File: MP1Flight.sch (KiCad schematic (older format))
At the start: 43 parts, among them J3 Micro_SD_Card_Det, J6 Conn_01x04_Male, J7 Screw_Terminal_01x02, SW1 SW_Push, U1 MPU-9250, U2 VisionSOM-STM32MP1

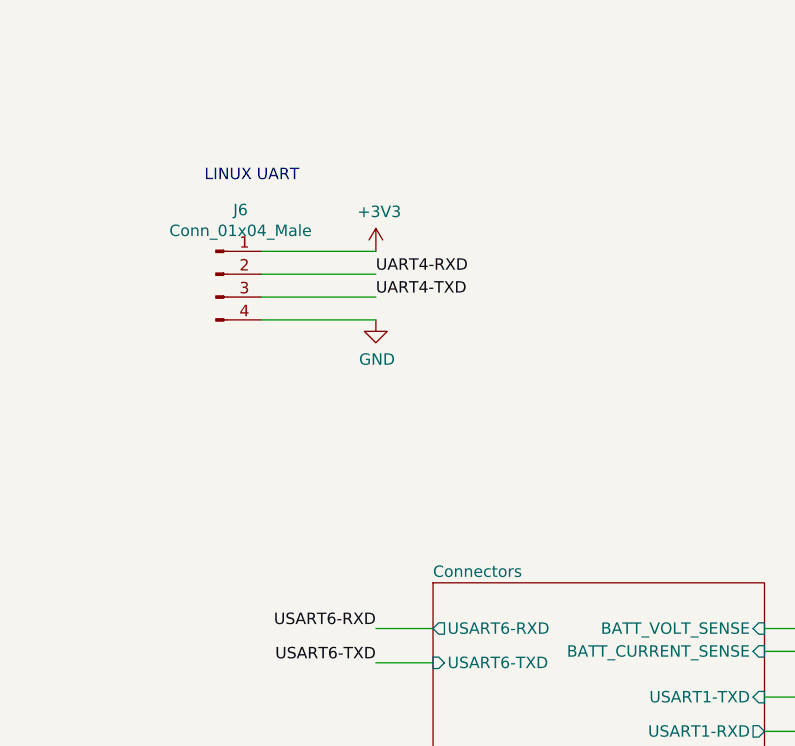
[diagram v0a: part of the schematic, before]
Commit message: Added in Debug sheet
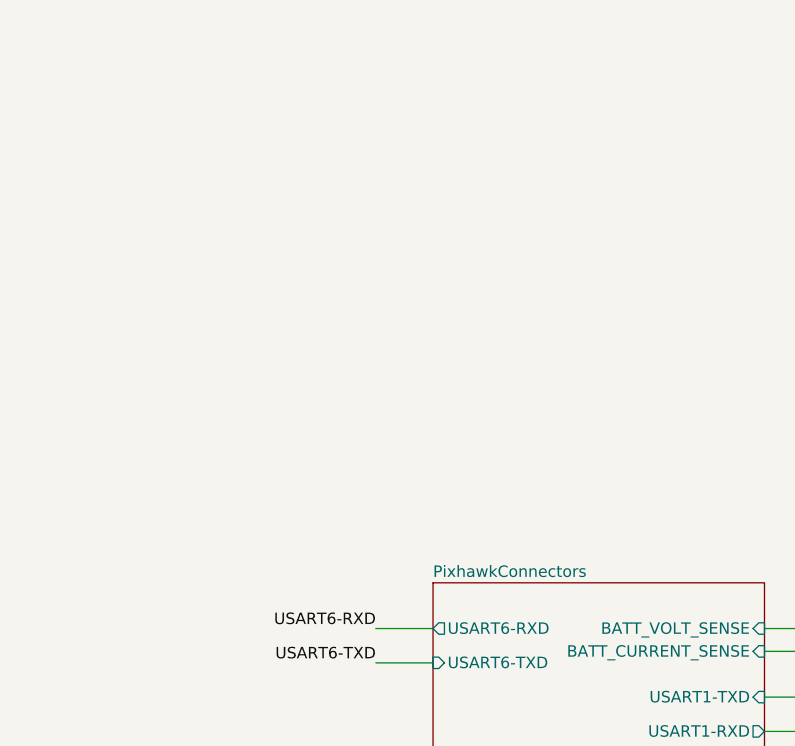
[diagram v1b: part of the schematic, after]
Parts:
- removed J6: Conn_01x04_Male, symbol Connector:Conn_01x04_Male
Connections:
- wire segments 152 -> 148
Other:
- note removed: "LINUX UART"
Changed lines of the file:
@@
 Text Notes 15500 9750 0    50   ~ 0
 LCD NOT BEING USED
-Text Label 2100 7150 0    50   ~ 0
-UART4-TXD
-Text Label 2100 7050 0    50   ~ 0
-UART4-RXD
-$Comp
-L power:+3V3 #PWR0149
-U 1 1 5EF84678
-P 2100 6950
-F 0 "#PWR0149" H 2100 6800 50  0001 C CNN
-F 1 "+3V3" H 2115 7123 50  0000 C CNN
-F 2 "" H 2100 6950 50  0001 C CNN
-F 3 "" H 2100 6950 50  0001 C CNN
-	1    2100 6950
-	1    0    0    -1
-$EndComp
-$Comp
-L power:GND #PWR0148
-U 1 1 5EF827E4
-P 2100 7250
-F 0 "#PWR0148" H 2100 7000 50  0001 C CNN
-F 1 "GND" H 2105 7077 50  0000 C CNN
-F 2 "" H 2100 7250 50  0001 C CNN
-F 3 "" H 2100 7250 50  0001 C CNN
-	1    2100 7250
-	1    0    0    -1
-$EndComp
-Wire Wire Line
-	1600 7250 2100 7250
-Wire Wire Line
-	1600 7150 2100 7150
-Wire Wire Line
-	1600 7050 2100 7050
-Wire Wire Line
-	1600 6950 2100 6950
-Text Notes 1350 6650 0    50   ~ 0
-LINUX UART
-$Comp
-L Connector:Conn_01x04_Male J6
-U 1 1 5EF08DF3
-P 1400 7050
-F 0 "J6" H 1508 7331 50  0000 C CNN
-F 1 "Conn_01x04_Male" H 1508 7240 50  0000 C CNN
-F 2 "" H 1400 7050 50  0001 C CNN
-F 3 "~" H 1400 7050 50  0001 C CNN
-	1    1400 7050
-	1    0    0    -1
-$EndComp
 $Sheet
 S 1550 2550 1350 1850
@@
 S 2350 8400 1450 1550
 U 5ED8E7B0
-F0 "Connectors" 50
+F0 "PixhawkConnectors" 50
 F1 "Connectors.sch" 50
 F2 "USART1-TXD" I R 3800 8900 50

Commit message: Added in SD Card Sheet plus made SD card connections
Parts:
- removed C14, C22, C24: 10uF, symbol Device:C
- removed C20: 1uF, symbol Device:C
- removed C21: 100nF, Capacitor_SMD:C_0603_1608Metric_Pad1.05x0.95mm_HandSolder, symbol Device:C
- removed C23, C25: 100nF, symbol Device:C
- removed C6: 100uF, Capacitor_Tantalum_SMD:CP_EIA-2012-15_AVX-P_Pad1.30x1.05mm_HandSolder, symbol Device:C
- removed D2: PMEG2020CPA,115, PMEG2020CPA115, symbol PMEG2020CPA_115:PMEG2020CPA,115
- removed F1, F2: 2A, symbol Device:Fuse
- removed J3: Micro_SD_Card_Det, symbol Connector:Micro_SD_Card_Det
- removed J7: Screw_Terminal_01x02, symbol Connector:Screw_Terminal_01x02
- removed R8: 12k, Resistor_SMD:R_0603_1608Metric_Pad1.05x0.95mm_HandSolder, symbol Device:R
- removed R9: 10k, symbol Device:R
- removed SS1: BD2242G-GTR, SOT95P280X125-6N, symbol BD2242G-GTR:BD2242G-GTR
- removed TP1: TestPoint, TestPoint:TestPoint_Plated_Hole_D3.0mm, symbol Connector:TestPoint
- removed Z1: 1SMA5919BT3G, DIOM5226X220N, symbol 1SMA5919BT3G:1SMA5919BT3G
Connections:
- net labels added: MISO, MOSI, SCLK, SD2-CLK, SD2-CMD, SD2-DATA0, SD2-DATA1, SD2-DATA2, SD2-DATA3
- net labels removed: MPU9250_SCLK, VDD_SDCARD
- wire segments 148 -> 118
- no-connect marks 2 -> 4

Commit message: Added in Servo Outputs and Setup the timers in CubeMX
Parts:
- removed C10, C9: 100nF, Capacitor_SMD:C_0603_1608Metric_Pad1.05x0.95mm_HandSolder, symbol Device:C
- removed C8: 2.2uF, symbol Device:C
- removed D1: LED, LED_SMD:LED_0603_1608Metric_Pad1.05x0.95mm_HandSolder, symbol Device:LED
- removed R1: 330, Resistor_SMD:R_0603_1608Metric_Pad1.05x0.95mm_HandSolder, symbol Device:R
- removed U1: MPU-9250, Sensor_Motion:InvenSense_QFN-24_3x3mm_P0.4mm, symbol Sensor_Motion:MPU-9250
- added F3: 0.65A, symbol Device:Fuse
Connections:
- net labels added: PWM1, PWM2, PWM3, PWM4, PWM5, PWM6, SCLk
- net labels removed: +3V3, MPU9250_MISO, MPU9250_MOSI
- wire segments 118 -> 100
- no-connect marks 4 -> 2

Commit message: Added in Buzzer and N channel mosfet
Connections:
- net labels added: FRSKY_INV, VOUT-3V3
- net labels removed: +3.3V
- wire segments 100 -> 102
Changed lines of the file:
@@
 Connection ~ 15350 4300
-$Comp
-L power:+3.3V #PWR0118
-U 1 1 5ED0729F
-P 14850 4550
-F 0 "#PWR0118" H 14850 4400 50  0001 C CNN
-F 1 "+3.3V" H 14865 4723 50  0000 C CNN
-F 2 "" H 14850 4550 50  0001 C CNN
-F 3 "" H 14850 4550 50  0001 C CNN
-	1    14850 4550
-	1    0    0    -1
-$EndComp
 $Comp
 L power:VDD #PWR0121
@@
 F11 "USART6-TXD" I L 1850 6400 50
 F12 "USART6-RXD" O L 1850 6250 50
+F13 "FRSKY_INV" I L 1850 6750 50
 $EndSheet
 Text Label 1600 6250 2    50   ~ 0
@@
 Wire Wire Line
 	14550 4550 14850 4550
-Connection ~ 14850 4550
 Text Label 9200 4350 0    50   ~ 0
 MPU9250_DRDY
@@
 Text Label 3300 8400 0    50   ~ 0
 PWM6
+Text Label 14850 4550 0    50   ~ 0
+VOUT-3V3
+Text Label 12350 5450 2    50   ~ 0
+FRSKY_INV
+Wire Wire Line
+	13150 5450 12350 5450
+Wire Wire Line
+	1850 6750 1600 6750
+Text Label 1600 6750 2    50   ~ 0
+FRSKY_INV
 $EndSCHEMATC

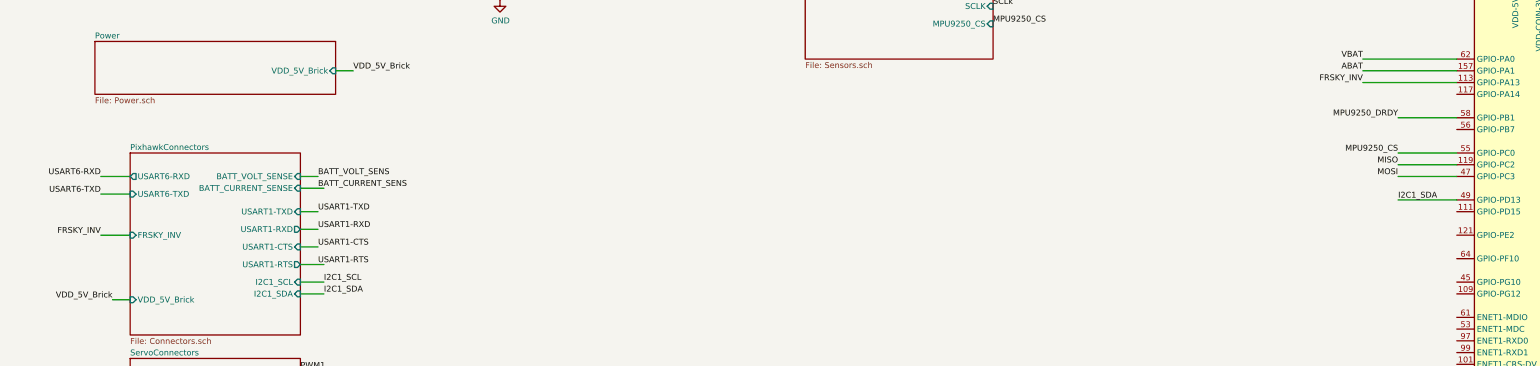
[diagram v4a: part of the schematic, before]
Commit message: Safety LED, Alarm and Safety switch additions
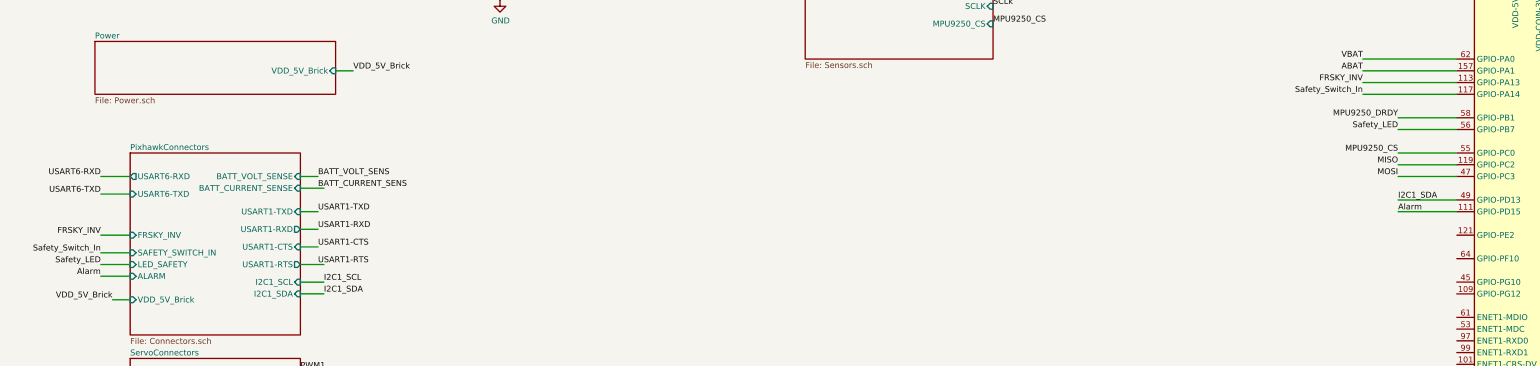
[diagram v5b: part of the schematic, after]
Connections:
- net labels added: Alarm, Safety_LED, Safety_Switch_In
- wire segments 102 -> 108
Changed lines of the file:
@@
 F12 "USART6-RXD" O L 1850 6250 50
 F13 "FRSKY_INV" I L 1850 6750 50
+F14 "SAFETY_SWITCH_IN" I L 1850 6900 50
+F15 "LED_SAFETY" I L 1850 7000 50
+F16 "ALARM" I L 1850 7100 50
 $EndSheet
 Text Label 1600 6250 2    50   ~ 0
@@
 Text Label 1600 6750 2    50   ~ 0
 FRSKY_INV
+Text Label 12350 5550 2    50   ~ 0
+Safety_Switch_In
+Wire Wire Line
+	12350 5550 13150 5550
+Wire Wire Line
+	1600 6900 1850 6900
+Text Label 1600 6900 2    50   ~ 0
+Safety_Switch_In
+Wire Wire Line
+	13150 5850 12650 5850
+Text Label 12650 5850 2    50   ~ 0
+Safety_LED
+Wire Wire Line
+	1850 7000 1600 7000
+Text Label 1600 7000 2    50   ~ 0
+Safety_LED
+Wire Wire Line
+	1850 7100 1600 7100
+Text Label 1600 7100 2    50   ~ 0
+Alarm
+Wire Wire Line
+	12650 6550 13150 6550
+Text Label 12650 6550 0    50   ~ 0
+Alarm
 $EndSCHEMATC

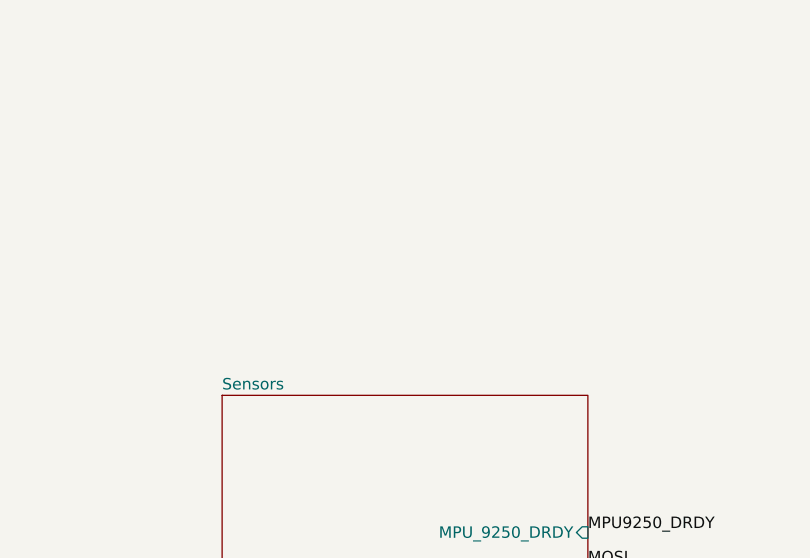
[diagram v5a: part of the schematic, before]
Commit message: IMU1/2 added in plus regs
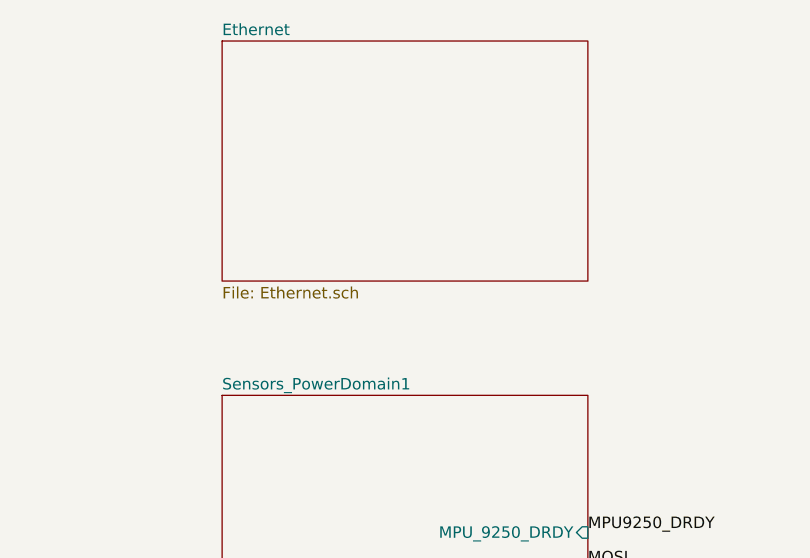
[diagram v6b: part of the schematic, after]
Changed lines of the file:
@@
 $Descr A2 23386 16535
 encoding utf-8
-Sheet 1 7
+Sheet 1 8
 Title "MP1Flight"
 Date "1"
@@
 S 7600 3750 1600 1500
 U 5F064FD4
-F0 "Sensors" 50
+F0 "Sensors_PowerDomain1" 50
 F1 "Sensors.sch" 50
 F2 "MPU_9250_DRDY" I R 9200 4350 50
@@
 Text Label 12650 6550 0    50   ~ 0
 Alarm
+$Sheet
+S 7600 2200 1600 1050
+U 5ED4AD57
+F0 "Ethernet" 50
+F1 "Ethernet.sch" 50
+$EndSheet
 $EndSCHEMATC
